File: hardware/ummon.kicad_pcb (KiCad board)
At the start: 4 copper layers, 60 x 60 mm, 94 parts, among them J2 Conn_01x05_Pin, J3 Conn_01x04_Pin, J4 Conn_01x04_Pin, J5 Conn_01x04_Pin, J6 Conn_01x09_Pin, P1 Display, Q1 BSS138LT1G, Q2 AO3401A, Q3 AO3401A, SW1 Reboot, SW2 Flash, SW3 Test Button, SW4 MINI MSK12CO2, U1 ESP32-C6-WROOM-1-N8, U2 SCD41, U3 SGP41, U4 SHT41, U5 AMS1117-3.3, U6 10μH

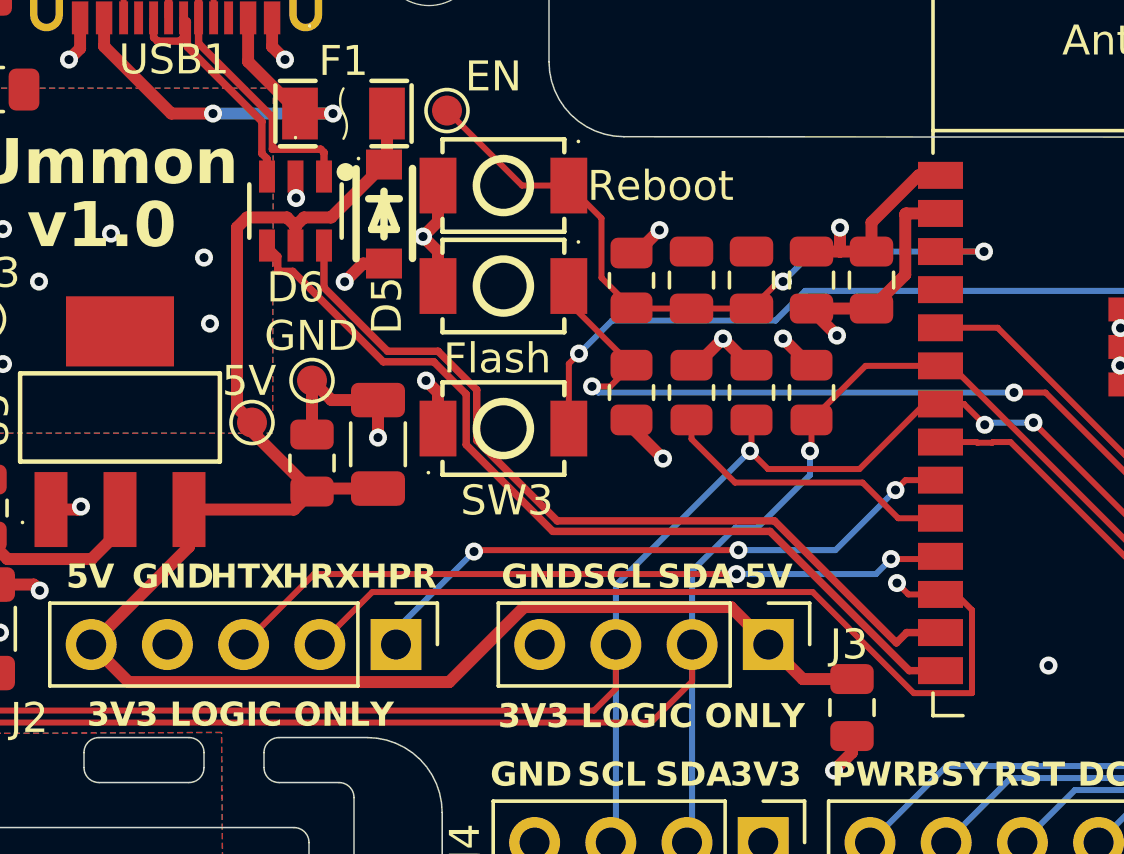
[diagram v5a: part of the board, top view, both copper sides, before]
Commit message: :bug: Fix usb net names swapped and add 100nF C to D6
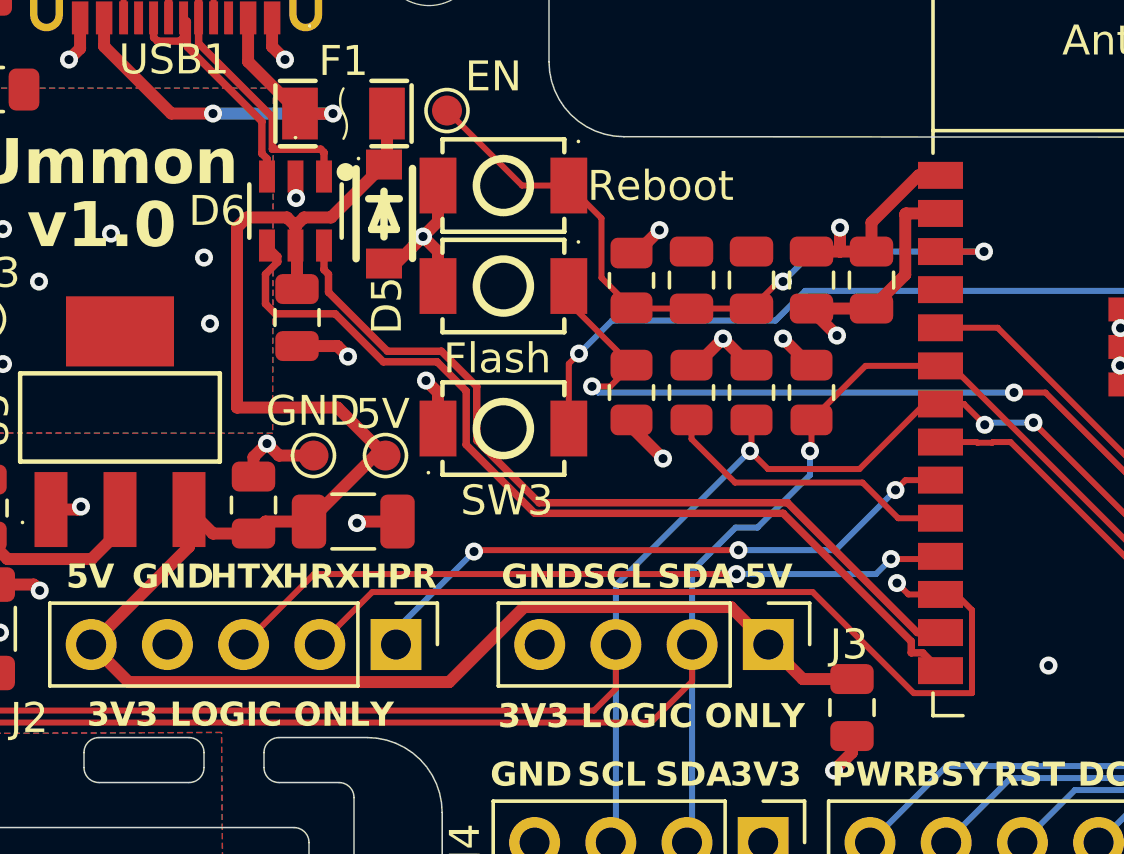
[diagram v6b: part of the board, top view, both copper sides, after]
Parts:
- added C20: 100nF, Capacitor_SMD:C_0805_2012Metric, F.Cu at (127.1, 106.0)
- moved TP8 4.58 mm to (130.1, 110.6)
- moved C14 2.70 mm to (129.0, 112.8), turned to 0 degrees
- moved TP9 2.50 mm to (127.7, 110.6)
- moved C15 2.40 mm to (125.7, 112.2)
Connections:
- D6 pad 1: /USB_PORT_D+ -> /USB_PORT_D-
- D6 pad 3: /USB_PORT_D- -> /USB_PORT_D+
- USB1 pad A6: /USB_PORT_D- -> /USB_PORT_D+
- USB1 pad A7: /USB_PORT_D+ -> /USB_PORT_D-
- USB1 pad B6: /USB_PORT_D- -> /USB_PORT_D+
- USB1 pad B7: /USB_PORT_D+ -> /USB_PORT_D-
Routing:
- net +5V: track 58.6 -> 63.2 mm
- net /USB_PORT_D-: track 8.85 -> 10.4 mm
- net /USB_PORT_D+: track 10.4 -> 8.85 mm
- net /USB_D+: track 29.6 -> 31.1 mm
- net GND: track 146.5 -> 147.3 mm, vias 59 -> 60

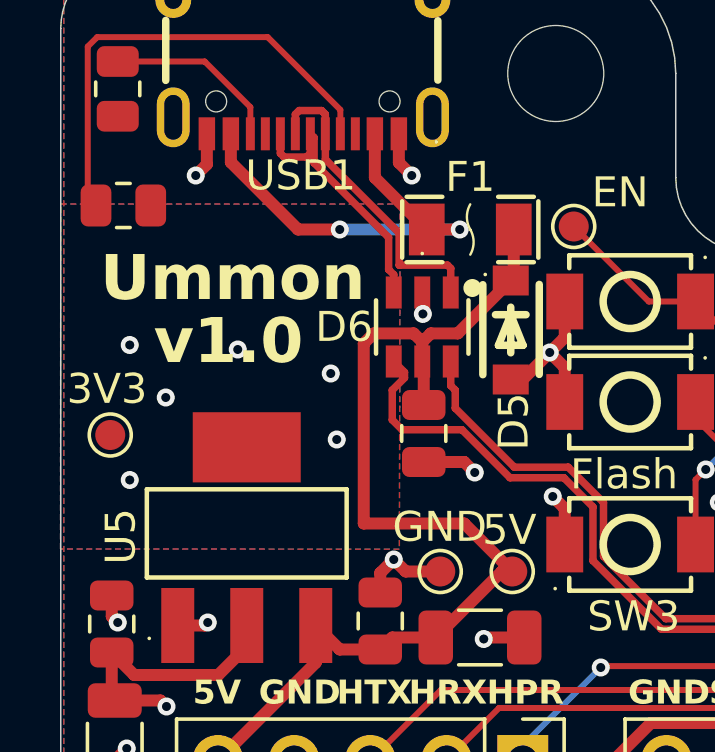
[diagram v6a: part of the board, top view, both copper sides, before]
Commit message: :zap: Increase LDO thermal zone size
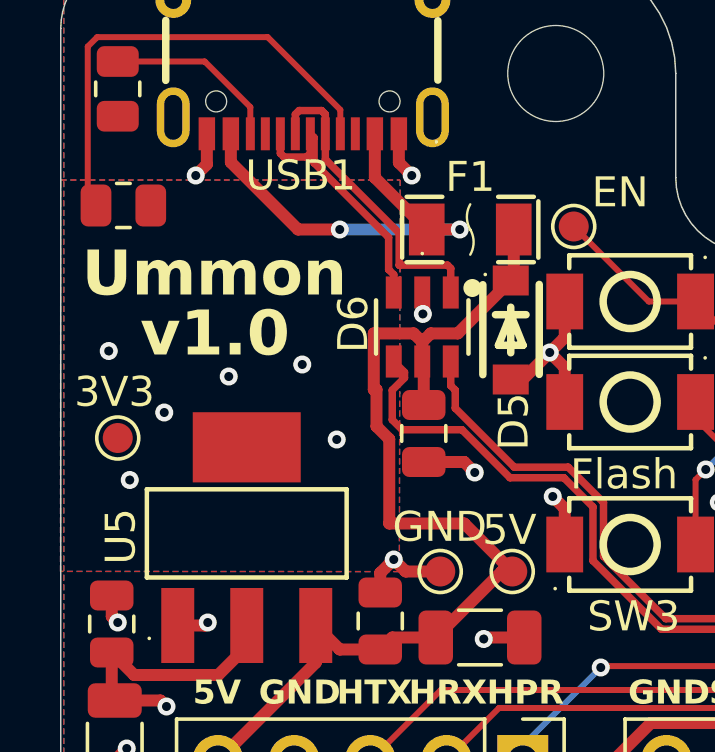
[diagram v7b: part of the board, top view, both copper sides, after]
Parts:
- moved TP2 0.27 mm to (116.9, 106.2)
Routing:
- net +5V: track 63.2 -> 62.5 mm
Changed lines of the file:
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@@
 	(footprint "TestPoint:TestPoint_Pad_D1.0mm"
 		(layer "F.Cu")
-		(at 116.65 106.05)
+		(at 116.9 106.15)
 		(descr "SMD pad as test Point, diameter 1.0mm")
 		(tags "test point SMD pad")
@@
 		(descr "USBLC6-2SC6")
 		(property "Reference" "D6"
-			(at 2.6 0 0)
+			(at 2.3 0.1 90)
 			(layer "F.SilkS")
 			(effects
@@
 	)
 	(gr_text "Ummon"
-		(at 116.314285 101.7 0)
+		(at 115.7 101.55 0)
 		(layer "F.SilkS")
 		(effects
@@
 	)
 	(gr_text "v1.0"
-		(at 118.1 103.8 0)
+		(at 117.65 103.55 0)
 		(layer "F.SilkS")
 		(effects
@@
 	)
 	(via
-		(at 120.9 103.2)
-		(size 0.6)
-		(drill 0.3)
-		(layers "F.Cu" "B.Cu")
-		(net "+3.3V")
-	)
-	(via
-		(at 117.3 103.05)
+		(at 120.6 104.1)
 		(size 0.6)
 		(drill 0.3)
@@
 	)
 	(via
-		(at 124 104)
+		(at 123.05 103.7)
 		(size 0.6)
 		(drill 0.3)
@@
 	)
 	(via
+		(at 118.45 105.3)
+		(size 0.6)
+		(drill 0.3)
+		(layers "F.Cu" "B.Cu")
+		(net "+3.3V")
+	)
+	(via
 		(at 124.2 106.2)
 		(size 0.6)
@@
 	)
 	(via
-		(at 118.5 104.8)
+		(at 116.6 103.25)
 		(size 0.6)
 		(drill 0.3)
@@
 	)
 	(segment
-		(start 126.766 102.664)
-		(end 125.434 102.664)
+		(start 125.95 109.000001)
+		(end 128.450001 109.000001)
 		(width 0.4)
 		(layer "F.Cu")
@@
 	)
 	(segment
-		(start 125.100001 109.000001)
-		(end 128.450001 109.000001)
+		(start 125.525 104.536)
+		(end 125.525 105.762562)
+		(width 0.4)
+		(layer "F.Cu")
+		(net "+5V")
+	)
+	(segment
+		(start 125.434 102.664)
+		(end 125.434 104.536)
 		(width 0.4)
 		(layer "F.Cu")
@@
 	)
 	(segment
-		(start 128.450001 109.000001)
-		(end 130.05 110.6)
+		(start 127.1 103.65)
+		(end 127.05 103.6)
 		(width 0.4)
 		(layer "F.Cu")
@@
 	)
 	(segment
-		(start 127.1 103.65)
-		(end 127.05 103.6)
+		(start 130 100.9)
+		(end 128.236 102.664)
 		(width 0.4)
 		(layer "F.Cu")
@@
 	)
 	(segment
-		(start 130 100.9)
-		(end 128.236 102.664)
+		(start 128.450001 109.000001)
+		(end 130.05 110.6)
 		(width 0.4)
 		(layer "F.Cu")
@@
 	)
 	(segment
-		(start 126.766 102.664)
-		(end 127.05 102.948)
+		(start 125.525 105.762562)
+		(end 125.95 106.187562)
 		(width 0.4)
 		(layer "F.Cu")
@@
 	)
 	(segment
-		(start 125.65 113.2)
-		(end 124.3 113.2)
+		(start 127.05 102.948)
+		(end 126.766 102.664)
 		(width 0.4)
 		(layer "F.Cu")
@@
 	)
 	(segment
-		(start 120.24 116.9)
-		(end 121.49 118.15)
+		(start 125.95 106.187562)
+		(end 125.95 109.000001)
+		(width 0.4)
+		(layer "F.Cu")
+		(net "+5V")
+	)
+	(segment
+		(start 125.65 113.2)
+		(end 124.3 113.2)
 		(width 0.4)
 		(layer "F.Cu")
@@
 	)
 	(segment
-		(start 125.100001 102.997999)
-		(end 125.100001 109.000001)
+		(start 120.24 116.9)
+		(end 121.49 118.15)
 		(width 0.4)
 		(layer "F.Cu")
@@
 	)
 	(segment
-		(start 145.6 118.05)
-		(end 143.96 118.05)
+		(start 126.766 102.664)
+		(end 125.434 102.664)
 		(width 0.4)
 		(layer "F.Cu")
@@
 	)
 	(segment
-		(start 125.434 102.664)
-		(end 125.100001 102.997999)
+		(start 125.434 104.536)
+		(end 125.525 104.536)
+		(width 0.4)
+		(layer "F.Cu")
+		(net "+5V")
+	)
+	(segment
+		(start 145.6 118.05)
+		(end 143.96 118.05)
 		(width 0.4)
 		(layer "F.Cu")
@@
 		(polygon
 			(pts
-				(xy 126.287678 109.856626) (xy 114.991185 109.849712) (xy 114.998225 98.353079) (xy 126.312304 98.353079)
+				(xy 126.286079 110.603449) (xy 114.990728 110.596536) (xy 114.998717 97.55) (xy 126.314023 97.55)
 			)
 		)

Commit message: :bug: EPD_PWR no longer uses strapping pin 15
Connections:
- J6 pad 9: /EPD_PWR -> /EPD_PWR_N
- R18 pad 2: /EPD_PWR -> /EPD_PWR_N
- SW3 pad 1: /GPIO3 -> /GPIO8
- U1 pad 23: /EPD_PWR -> unconnected-(U1-IO15-Pad23)
- U1 pad 26: /GPIO3 -> /EPD_PWR_N
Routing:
- net /EPD_PWR_N: track 0.00 -> 62.9 mm, vias 0 -> 2
- net /EPD_PWR: track 59.1 -> 0.00 mm, vias 2 -> 0
- net /GPIO3: track 33.6 -> 0.00 mm, vias 2 -> 0
- net /GPIO8: track 10.0 -> 16.3 mm
- net /H_RX: track 29.5 -> 27.9 mm, vias 1 -> 0
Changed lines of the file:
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@@
 			(size 1.5 0.9)
 			(layers "F.Cu" "F.Mask" "F.Paste")
-			(net "/EPD_PWR")
+			(net "unconnected-(U1-IO15-Pad23)")
 			(pinfunction "IO15_23")
-			(pintype "unspecified")
+			(pintype "unspecified+no_connect")
 		)
 		(pad "24" smd rect
@@
 			(size 1.5 0.9)
 			(layers "F.Cu" "F.Mask" "F.Paste")
-			(net "/GPIO3")
+			(net "/EPD_PWR_N")
 			(pinfunction "IO3_26")
 			(pintype "unspecified")
@@
 			)
 		)
+		(attr exclude_from_bom)
 		(duplicate_pad_numbers_are_jumpers no)
 		(fp_circle
@@
 			)
 		)
+		(attr exclude_from_bom)
 		(duplicate_pad_numbers_are_jumpers no)
 		(fp_circle
@@
 			(layers "F.Cu" "F.Mask" "F.Paste")
 			(roundrect_rratio 0.243902)
-			(net "/EPD_PWR")
+			(net "/EPD_PWR_N")
 			(pintype "passive")
 		)
@@
 			(size 1.23 1.86)
 			(layers "F.Cu" "F.Mask" "F.Paste")
-			(net "/GPIO3")
+			(net "/GPIO8")
 			(pinfunction "1_1")
 			(pintype "unspecified")
@@
 			)
 		)
+		(attr exclude_from_bom)
 		(duplicate_pad_numbers_are_jumpers no)
 		(fp_circle
@@
 			)
 		)
+		(attr exclude_from_bom)
 		(duplicate_pad_numbers_are_jumpers no)
 		(fp_circle
@@
 			)
 		)
+		(attr exclude_from_bom)
 		(duplicate_pad_numbers_are_jumpers no)
 		(fp_circle
@@
 			)
 		)
+		(attr exclude_from_bom)
 		(duplicate_pad_numbers_are_jumpers no)
 		(fp_circle
@@
 			)
 		)
+		(attr exclude_from_bom)
 		(duplicate_pad_numbers_are_jumpers no)
 		(fp_circle
@@
 			)
 		)
+		(attr exclude_from_bom)
 		(duplicate_pad_numbers_are_jumpers no)
 		(fp_circle
@@
 			)
 		)
+		(attr exclude_from_bom)
 		(duplicate_pad_numbers_are_jumpers no)
 		(fp_circle
@@
 			)
 		)
-		(attr through_hole)
+		(attr through_hole exclude_from_bom)
 		(duplicate_pad_numbers_are_jumpers no)
 		(fp_line
@@
 			(layers "*.Cu" "*.Mask")
 			(remove_unused_layers no)
-			(net "/EPD_PWR")
+			(net "/EPD_PWR_N")
 			(pinfunction "Pin_9_9")
 			(pintype "passive")
@@
 			)
 		)
+		(attr exclude_from_bom)
 		(duplicate_pad_numbers_are_jumpers no)
 		(fp_circle
@@
 			)
 		)
+		(attr exclude_from_bom)
 		(duplicate_pad_numbers_are_jumpers no)
 		(fp_circle
@@
 		(tags "Through hole pin header THT 1x04 2.54mm single row")
 		(property "Reference" "J3"
-			(at 0 -2.69 180)
+			(at -0.2 -2.69 180)
 			(layer "F.SilkS")
 			(effects
@@
 	)
 	(segment
+		(start 139.548529 111.3)
+		(end 140.25 110.598529)
+		(width 0.2)
+		(layer "F.Cu")
+		(net "/GPIO8")
+	)
+	(segment
+		(start 137.76 111.3)
+		(end 139.548529 111.3)
+		(width 0.2)
+		(layer "F.Cu")
+		(net "/GPIO8")
+	)
+	(segment
+		(start 140.25 110.598529)
+		(end 140.25 109.4125)
+		(width 0.2)
+		(layer "F.Cu")
+		(net "/GPIO8")
+	)
+	(segment
 		(start 148.55 112.69)
 		(end 147.14 112.69)
@@
 	)
 	(segment
+		(start 136.16 109.7)
+		(end 137.76 111.3)
+		(width 0.2)
+		(layer "F.Cu")
+		(net "/GPIO8")
+	)
+	(segment
 		(start 148.46 114.05)
 		(end 148.55 113.96)
@@
 	)
 	(segment
-		(start 147.48 115.23)
-		(end 147.1 114.85)
-		(width 0.2)
-		(layer "F.Cu")
-		(net "/H_RX")
-	)
-	(segment
 		(start 144.28906 115.15)
 		(end 147.65906 118.52)
@@
 	)
 	(segment
-		(start 148.55 115.23)
-		(end 147.48 115.23)
-		(width 0.2)
-		(layer "F.Cu")
-		(net "/H_RX")
-	)
-	(segment
 		(start 149.6 115.75)
 		(end 149.08 115.23)
@@
 		(net "/H_RX")
 	)
-	(via
-		(at 147.1 114.85)
-		(size 0.6)
-		(drill 0.3)
-		(layers "F.Cu" "B.Cu")
-		(net "/H_RX")
-	)
 	(segment
 		(start 135.170794 112.17302)
@@
 	)
 	(segment
-		(start 133.3 147.125)
-		(end 133.3 145.7)
-		(width 0.2)
-		(layer "F.Cu")
-		(net "/EPD_PWR")
-	)
-	(segment
-		(start 166.05 107.61)
-		(end 164.21 107.61)
-		(width 0.2)
-		(layer "F.Cu")
-		(net "/EPD_PWR")
-	)
-	(segment
-		(start 134.3 148.125)
-		(end 133.3 147.125)
-		(width 0.2)
-		(layer "F.Cu")
-		(net "/EPD_PWR")
-	)
-	(segment
-		(start 164.21 107.61)
-		(end 164.2 107.6)
-		(width 0.2)
-		(layer "F.Cu")
-		(net "/EPD_PWR")
-	)
-	(segment
-		(start 133.3 145.7)
-		(end 133.8 145.2)
-		(width 0.2)
-		(layer "F.Cu")
-		(net "/EPD_PWR")
-	)
-	(via
-		(at 133.8 145.2)
-		(size 0.6)
-		(drill 0.3)
-		(layers "F.Cu" "B.Cu")
-		(net "/EPD_PWR")
-	)
-	(via
-		(at 164.2 107.6)
-		(size 0.6)
-		(drill 0.3)
-		(layers "F.Cu" "B.Cu")
-		(net "/EPD_PWR")
-	)
-	(segment
-		(start 162.752157 109.047843)
-		(end 162.752157 112.870785)
-		(width 0.2)
-		(layer "B.Cu")
-		(net "/EPD_PWR")
-	)
-	(segment
-		(start 133.8 135.9)
-		(end 146.2 123.5)
-		(width 0.2)
-		(layer "B.Cu")
-		(net "/EPD_PWR")
-	)
-	(segment
-		(start 133.8 145.2)
-		(end 133.8 135.9)
-		(width 0.2)
-		(layer "B.Cu")
-		(net "/EPD_PWR")
-	)
-	(segment
-		(start 154.672942 120.95)
-		(end 148.75 120.95)
-		(width 0.2)
-		(layer "B.Cu")
-		(net "/EPD_PWR")
-	)
-	(segment
-		(start 164.2 107.6)
-		(end 162.752157 109.047843)
-		(width 0.2)
-		(layer "B.Cu")
-		(net "/EPD_PWR")
-	)
-	(segment
-		(start 162.752157 112.870785)
-		(end 154.672942 120.95)
-		(width 0.2)
-		(layer "B.Cu")
-		(net "/EPD_PWR")
-	)
-	(segment
-		(start 148.75 120.95)
-		(end 146.2 123.5)
-		(width 0.2)
-		(layer "B.Cu")
-		(net "/EPD_PWR")
-	)
-	(segment
 		(start 171.4 110.74)
 		(end 171.4 115.65)
@@
 	)
 	(segment
-		(start 164.1 103.9)
-		(end 165.95 103.9)
-		(width 0.2)
-		(layer "F.Cu")
-		(net "/GPIO3")
-	)
-	(segment
-		(start 165.95 103.9)
-		(end 166.05 103.8)
-		(width 0.2)
-		(layer "F.Cu")
-		(net "/GPIO3")
-	)
-	(segment
-		(start 136.16 109.7)
-		(end 136.16 107.54)
-		(width 0.2)
-		(layer "F.Cu")
-		(net "/GPIO3")
-	)
-	(segment
-		(start 136.16 107.54)
-		(end 136.5 107.2)
-		(width 0.2)
-		(layer "F.Cu")
-		(net "/GPIO3")
-	)
-	(via
-		(at 164.1 103.9)
-		(size 0.6)
-		(drill 0.3)
-		(layers "F.Cu" "B.Cu")
-		(net "/GPIO3")
-	)
-	(via
-		(at 136.5 107.2)
-		(size 0.6)
-		(drill 0.3)
-		(layers "F.Cu" "B.Cu")
-		(net "/GPIO3")
-	)
-	(segment
-		(start 143.051471 106.1)
-		(end 137.6 106.1)
-		(width 0.2)
-		(layer "B.Cu")
-		(net "/GPIO3")
-	)
-	(segment
-		(start 162.89 105.11)
-		(end 144.041471 105.11)
-		(width 0.2)
-		(layer "B.Cu")
-		(net "/GPIO3")
-	)
-	(segment
-		(start 164.1 103.9)
-		(end 162.89 105.11)
-		(width 0.2)
-		(layer "B.Cu")
-		(net "/GPIO3")
-	)
-	(segment
-		(start 144.041471 105.11)
-		(end 143.051471 106.1)
-		(width 0.2)
-		(layer "B.Cu")
-		(net "/GPIO3")
-	)
-	(segment
-		(start 137.6 106.1)
-		(end 136.5 107.2)
-		(width 0.2)
-		(layer "B.Cu")
-		(net "/GPIO3")
-	)
-	(segment
 		(start 173.25 139.1)
 		(end 173.75 139.1)
@@
 		(net "Net-(LED3-A)")
 	)
+	(segment
+		(start 133.3 147.125)
+		(end 133.3 145.7)
+		(width 0.2)
+		(layer "F.Cu")
+		(net "/EPD_PWR_N")
+	)
+	(segment
+		(start 164.1 103.9)
+		(end 165.95 103.9)
+		(width 0.2)
+		(layer "F.Cu")
+		(net "/EPD_PWR_N")
+	)
+	(segment
+		(start 165.95 103.9)
+		(end 166.05 103.8)
+		(width 0.2)
+		(layer "F.Cu")
+		(net "/EPD_PWR_N")
+	)
+	(segment
+		(start 134.3 148.125)
+		(end 133.3 147.125)
+		(width 0.2)
+		(layer "F.Cu")
+		(net "/EPD_PWR_N")
+	)
+	(segment
+		(start 133.3 145.7)
+		(end 133.8 145.2)
+		(width 0.2)
+		(layer "F.Cu")
+		(net "/EPD_PWR_N")
+	)
+	(via
+		(at 164.1 103.9)
+		(size 0.6)
+		(drill 0.3)
+		(layers "F.Cu" "B.Cu")
+		(net "/EPD_PWR_N")
+	)
+	(via
+		(at 133.8 145.2)
+		(size 0.6)
+		(drill 0.3)
+		(layers "F.Cu" "B.Cu")
+		(net "/EPD_PWR_N")
+	)
+	(segment
+		(start 162.752157 112.870785)
+		(end 162.752157 105.247843)
+		(width 0.2)
+		(layer "B.Cu")
+		(net "/EPD_PWR_N")
+	)
+	(segment
+		(start 133.8 135.9)
+		(end 146.2 123.5)
+		(width 0.2)
+		(layer "B.Cu")
+		(net "/EPD_PWR_N")
+	)
+	(segment
+		(start 148.75 120.95)
+		(end 154.672942 120.95)
+		(width 0.2)
+		(layer "B.Cu")
+		(net "/EPD_PWR_N")
+	)
+	(segment
+		(start 146.2 123.5)
+		(end 148.75 120.95)
+		(width 0.2)
+		(layer "B.Cu")
+		(net "/EPD_PWR_N")
+	)
+	(segment
+		(start 154.672942 120.95)
+		(end 162.752157 112.870785)
+		(width 0.2)
+		(layer "B.Cu")
+		(net "/EPD_PWR_N")
+	)
+	(segment
+		(start 133.8 145.2)
+		(end 133.8 135.9)
+		(width 0.2)
+		(layer "B.Cu")
+		(net "/EPD_PWR_N")
+	)
+	(segment
+		(start 162.752157 105.247843)
+		(end 164.1 103.9)
+		(width 0.2)
+		(layer "B.Cu")
+		(net "/EPD_PWR_N")
+	)
 	(zone
